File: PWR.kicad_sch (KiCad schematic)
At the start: 37 parts, among them IC1 LMR51460SQDRRRQ1, IC2 TPS628101HQWRWYRQ1, IC3 LP2951-50DRG4, Q1 CSD25483F4, Q2 CSD25483F4

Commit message: improved analogs
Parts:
- added C42, C46: 1uF, Capacitor_SMD:C_0603_1608Metric_Pad1.08x0.95mm_HandSolder, symbol Device:C
- added NT2: NetTie_2, NetTie:NetTie-2_SMD_Pad0.5mm, symbol Device:NetTie_2
- added R13: 100k, Resistor_SMD:R_0603_1608Metric_Pad0.98x0.95mm_HandSolder, symbol Device:R
- C36, C37, C40, C41: footprint Capacitor_SMD:C_0402_1005Metric_Pad0.74x0.62mm_HandSolder -> Capacitor_SMD:C_0603_1608Metric_Pad1.08x0.95mm_HandSolder
- C5: footprint Inductor_SMD:L_1206_3216Metric_Pad1.22x1.90mm_HandSolder -> Capacitor_SMD:C_0603_1608Metric_Pad1.08x0.95mm_HandSolder
- R1, R10, R11, R12, R2, R3, R4, R5, R6, R7, R8, R9: footprint Resistor_SMD:R_0402_1005Metric_Pad0.72x0.64mm_HandSolder -> Resistor_SMD:R_0603_1608Metric_Pad0.98x0.95mm_HandSolder
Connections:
- net +12V is gone; now on net 12V: C33.1, C34.1, C35.1, IC1.10 (VIN_1), IC1.11 (VIN_2), IC1.12 (VIN_3), IC1.9 (EN), R48.1
- net GND: now also C46.2, NT2.1
- net A5V: now reaches IC3.1 (OUTPUT)
- net A5V: now also IC3.2 (SENSE), C42.1
- net AGND: now reaches IC3.3 (SHUTDOWN)
- net AGND: now also IC3.4 (GND), C42.2, NT2.2
- net A5V_PG: now reaches IC3.5 (~{ERROR})
- net A5V_PG: now also R13.1
- net at IC3.6 (VTAP): now also IC3.7 (FEEDBACK)
- net 12V: now reaches IC3.8 (INPUT)
- net 12V: now also C46.1
- net +3V3 renamed 3V3
- net 3V3: now also R13.2
- net +5V renamed 5V
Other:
- moved on the sheet: IC3, R11, R12

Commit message: possible working power mux
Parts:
- removed C33, C34: 4.7uF, Capacitor_SMD:C_1210_3225Metric_Pad1.33x2.70mm_HandSolder, symbol Device:C
- removed C35, C36: 0.1uF, Capacitor_SMD:C_0603_1608Metric_Pad1.08x0.95mm_HandSolder, symbol Device:C
- removed C37: 33pF, Capacitor_SMD:C_0603_1608Metric_Pad1.08x0.95mm_HandSolder, symbol Device:C
- removed C38, C39: 47uF, Capacitor_SMD:C_1210_3225Metric_Pad1.33x2.70mm_HandSolder, symbol Device:C
- removed C40: 4.7nF, Capacitor_SMD:C_0603_1608Metric_Pad1.08x0.95mm_HandSolder, symbol Device:C
- removed C41: 10pF, Capacitor_SMD:C_0603_1608Metric_Pad1.08x0.95mm_HandSolder, symbol Device:C
- removed C42, C46: 1uF, Capacitor_SMD:C_0603_1608Metric_Pad1.08x0.95mm_HandSolder, symbol Device:C
- removed C5, C8: 22uF, Capacitor_SMD:C_0603_1608Metric_Pad1.08x0.95mm_HandSolder, symbol Device:C
- removed C6, C7: 22uF, Inductor_SMD:L_1206_3216Metric_Pad1.22x1.90mm_HandSolder, symbol Device:C
- removed IC1: LMR51460SQDRRRQ1, SON50P300X300X80-13N-D, symbol SamacSys_Parts:LMR51460SQDRRRQ1
- removed IC2: TPS628101HQWRWYRQ1, SamacSys_Parts:TPS6281008QWRWYRQ1, symbol SamacSys_Parts:TPS62810QWRWYRQ1
- removed IC3: LP2951-50DRG4, SOIC127P600X175-8N, symbol 0_SamacSys_Parts:LP2951-50DRG4
- removed L1: 0.47uH, INDPM7066X240N, symbol Device:L
- removed L3: 4.7uH, Inductor_SMD:L_Coilcraft_XAL7030-472, symbol Device:L
- removed NT1: NetTie_2, NetTie:NetTie-2_SMD_Pad0.5mm, symbol Device:NetTie_2
- removed Q1, Q2: CSD25483F4, SamacSys_Parts:CSD25483F4T, symbol SamacSys_Parts:CSD25483F4T
- removed R1, R11, R12, R13, R4, R6: 100k, Resistor_SMD:R_0603_1608Metric_Pad0.98x0.95mm_HandSolder, symbol Device:R
- removed R10: 19.6k, Resistor_SMD:R_0603_1608Metric_Pad0.98x0.95mm_HandSolder, symbol Device:R
- removed R2: 19.1k, Resistor_SMD:R_0603_1608Metric_Pad0.98x0.95mm_HandSolder, symbol Device:R
- removed R3: 1k, Resistor_SMD:R_0603_1608Metric_Pad0.98x0.95mm_HandSolder, symbol Device:R
- removed R5, R7: 10k, Resistor_SMD:R_0603_1608Metric_Pad0.98x0.95mm_HandSolder, symbol Device:R
- removed R8: 8.06k, Resistor_SMD:R_0603_1608Metric_Pad0.98x0.95mm_HandSolder, symbol Device:R
- removed R9: 88.7k, Resistor_SMD:R_0603_1608Metric_Pad0.98x0.95mm_HandSolder, symbol Device:R
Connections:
- no-connect marks 1 -> 0
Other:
- added sheet PWR_3V3 (PWR_3V3.kicad_sch)
- added sheet PWR_A5V (PWR_A5V.kicad_sch)
- added sheet PWR_LV_5V (PWR_LV_5V.kicad_sch)
- added sheet PWR_MUX (PWR_MUX.kicad_sch)
- moved on the sheet: D14, D15, R48, R49

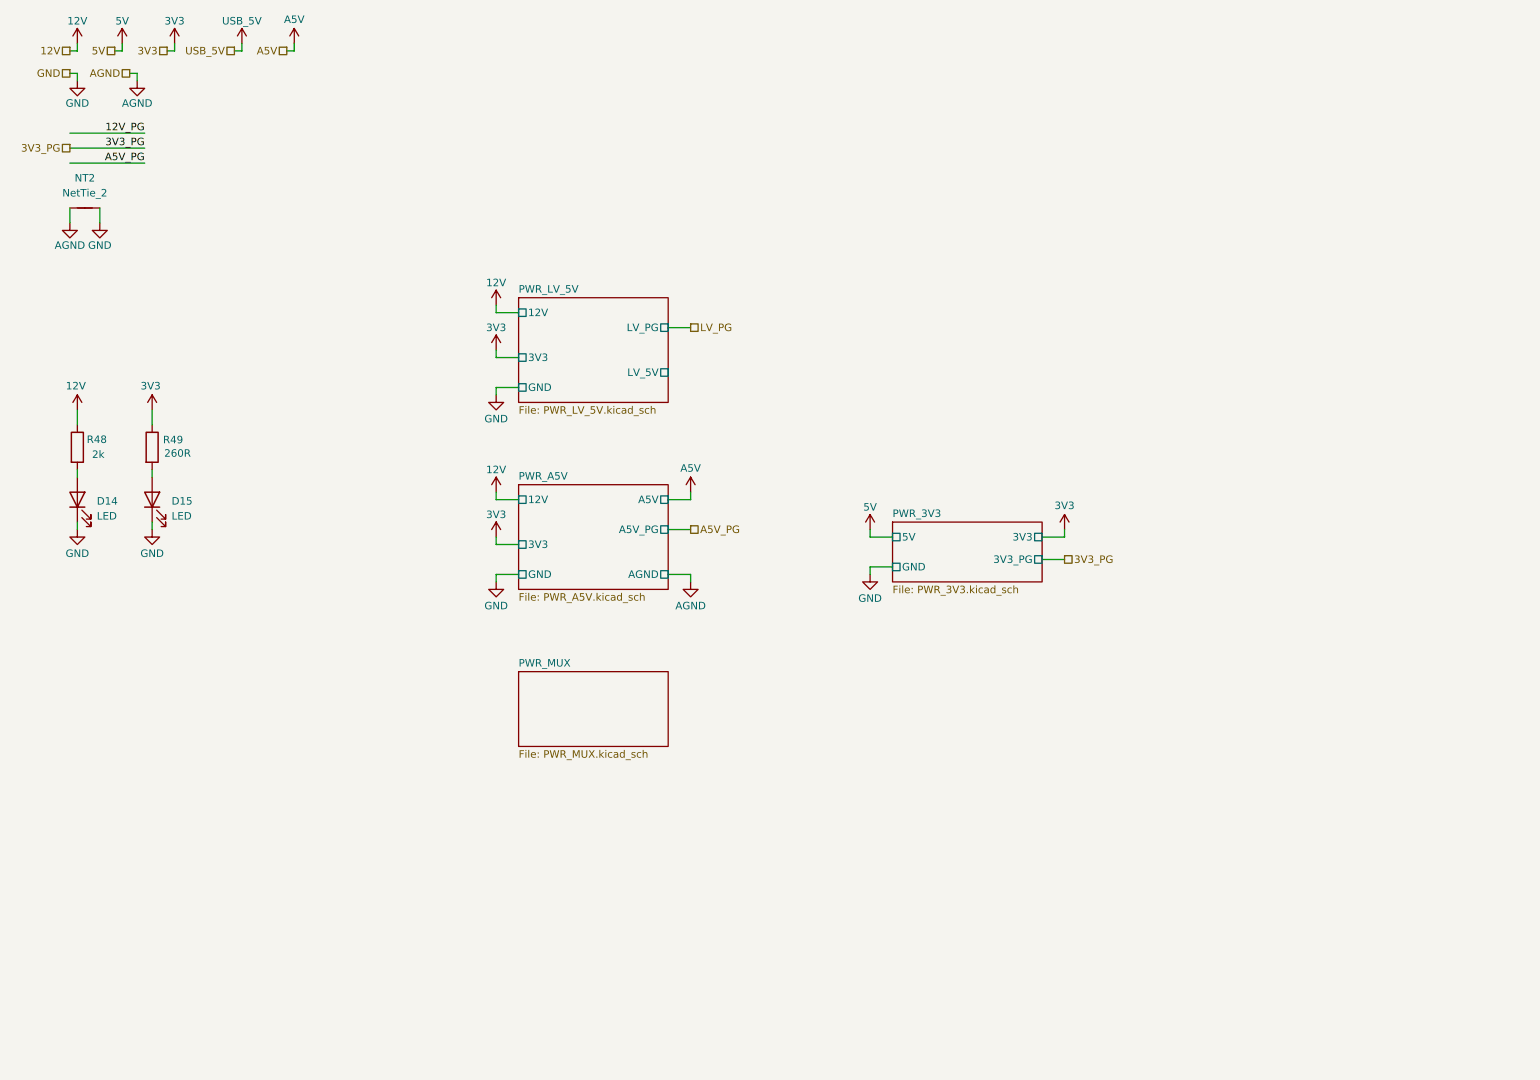
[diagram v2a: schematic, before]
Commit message: updated power layout
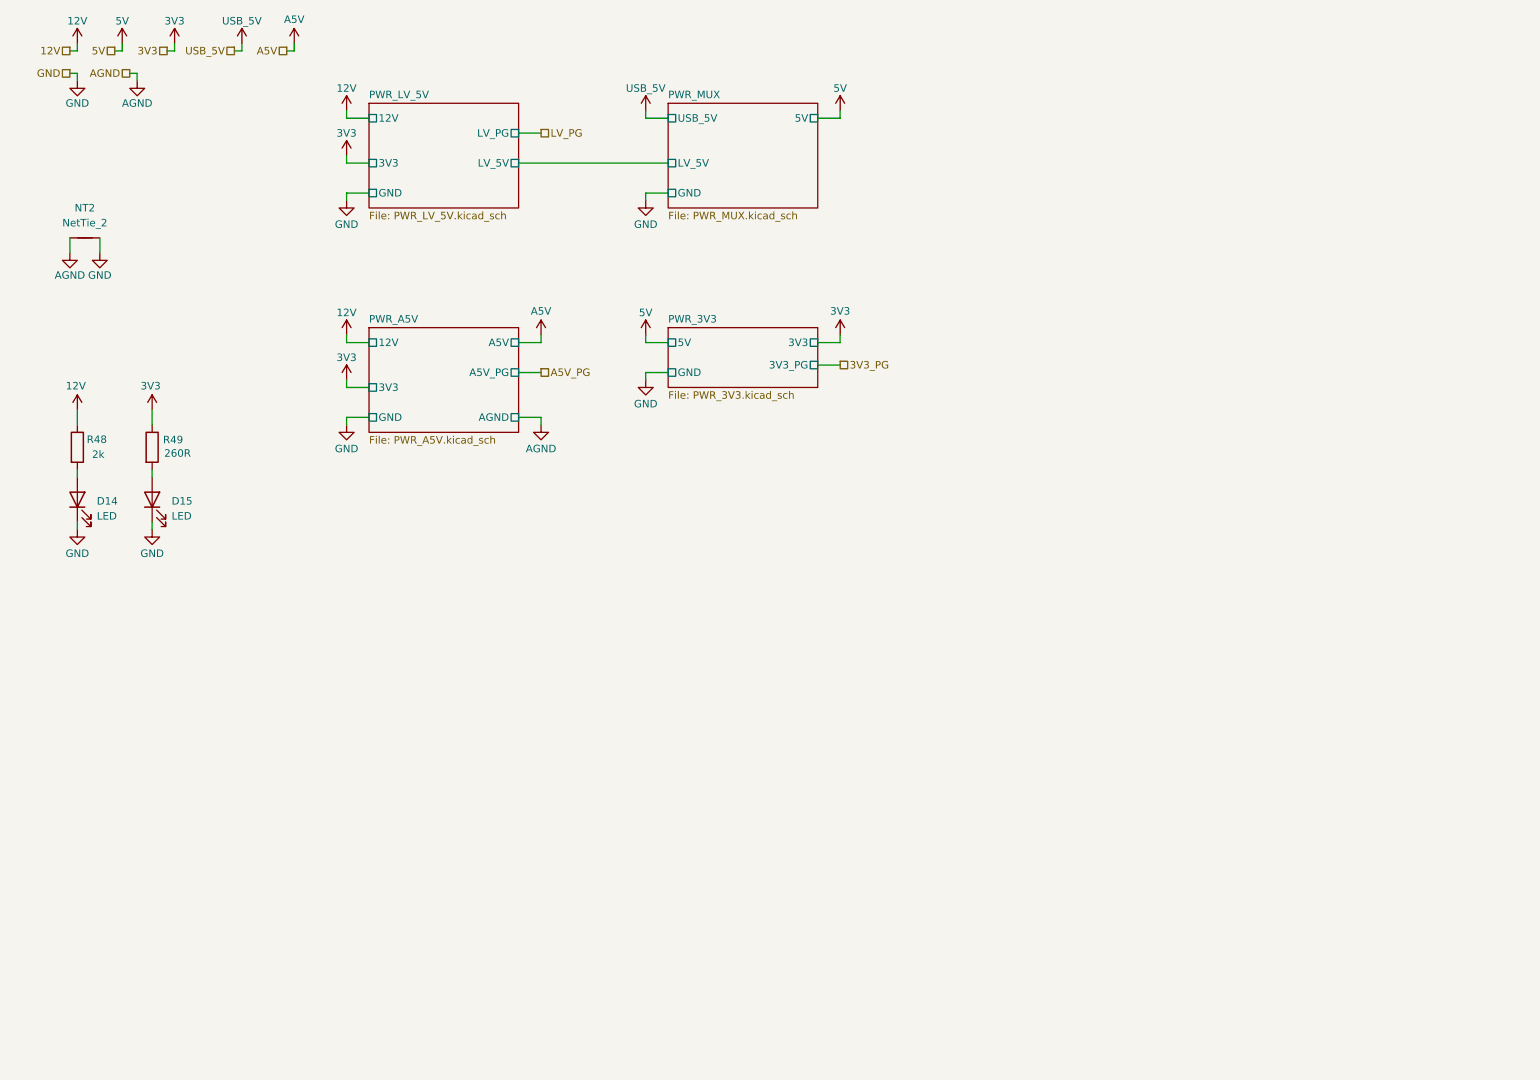
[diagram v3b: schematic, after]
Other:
- sheet PWR_MUX ports: added 5V, GND, LV_5V, USB_5V; removed none
- moved on the sheet: NT2

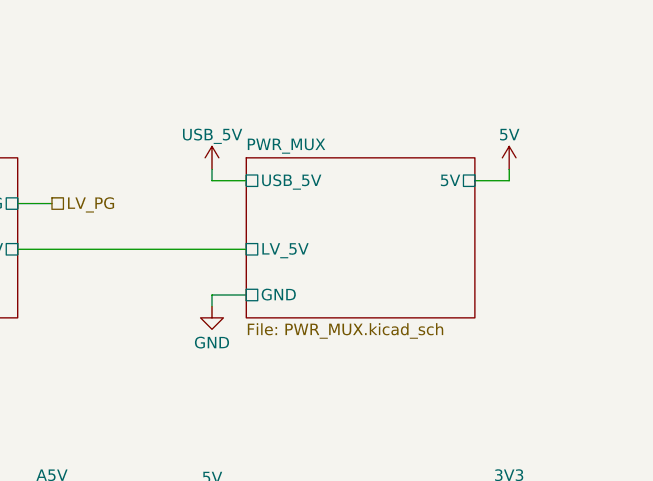
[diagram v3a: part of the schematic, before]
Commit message: added dip switches to wireless disables
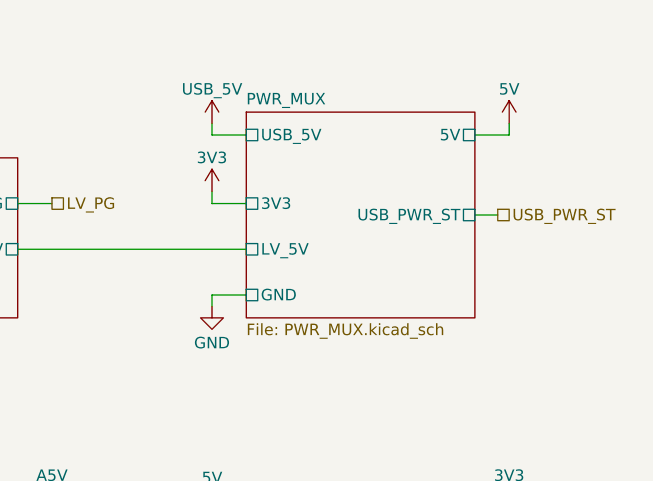
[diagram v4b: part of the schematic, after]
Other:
- sheet PWR_MUX ports: added 3V3, USB_PWR_ST; removed none
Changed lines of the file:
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@@
 	(wire
 		(pts
-			(xy 123.19 31.75) (xy 123.19 33.02)
+			(xy 123.19 26.67) (xy 123.19 27.94)
+		)
+		(stroke
+			(width 0)
+			(type default)
+		)
+	)
+	(wire
+		(pts
+			(xy 123.19 34.29) (xy 123.19 35.56)
 		)
 		(stroke
@@
 	(wire
 		(pts
-			(xy 156.21 31.75) (xy 156.21 33.02)
+			(xy 156.21 26.67) (xy 156.21 27.94)
 		)
 		(stroke
@@
 	(wire
 		(pts
+			(xy 123.19 35.56) (xy 127 35.56)
+		)
+		(stroke
+			(width 0)
+			(type default)
+		)
+	)
+	(wire
+		(pts
 			(xy 72.39 71.12) (xy 76.2 71.12)
 		)
@@
 	(wire
 		(pts
-			(xy 156.21 33.02) (xy 152.4 33.02)
+			(xy 156.21 27.94) (xy 152.4 27.94)
 		)
 		(stroke
@@
 	(wire
 		(pts
-			(xy 123.19 33.02) (xy 127 33.02)
+			(xy 123.19 27.94) (xy 127 27.94)
 		)
 		(stroke
@@
 		(pts
 			(xy 63.5 21.59) (xy 63.5 20.32)
+		)
+		(stroke
+			(width 0)
+			(type default)
+		)
+	)
+	(wire
+		(pts
+			(xy 152.4 36.83) (xy 154.94 36.83)
 		)
 		(stroke
@@
 		)
 	)
+	(hierarchical_label "USB_PWR_ST"
+		(shape passive)
+		(at 154.94 36.83 0)
+		(effects
+			(font
+				(size 1.27 1.27)
+			)
+			(justify left)
+		)
+	)
 	(hierarchical_label "5V"
 		(shape passive)
@@
 	)
 	(symbol
+		(lib_id "power:+12V")
+		(at 123.19 34.29 0)
+		(unit 1)
+		(exclude_from_sim no)
+		(in_bom yes)
+		(on_board yes)
+		(dnp no)
+		(property "Reference" "#PWR0310"
+			(at 123.19 38.1 0)
+			(effects
+				(font
+					(size 1.27 1.27)
+				)
+				(hide yes)
+			)
+		)
+		(property "Value" "3V3"
+			(at 123.19 30.48 0)
+			(effects
+				(font
+					(size 1.27 1.27)
+				)
+			)
+		)
+		(property "Footprint" ""
+			(at 123.19 34.29 0)
+			(effects
+				(font
+					(size 1.27 1.27)
+				)
+				(hide yes)
+			)
+		)
+		(property "Datasheet" ""
+			(at 123.19 34.29 0)
+			(effects
+				(font
+					(size 1.27 1.27)
+				)
+				(hide yes)
+			)
+		)
+		(property "Description" "Power symbol creates a global label with name \"+12V\""
+			(at 123.19 34.29 0)
+			(effects
+				(font
+					(size 1.27 1.27)
+				)
+				(hide yes)
+			)
+		)
+		(pin "1"
+		)
+		(instances
+			(project "NCU"
+				(path "/3aee14c3-5480-4f7c-989e-3fef81779034/05e3be97-98f6-4518-a1a7-240d4da327e6"
+					(reference "#PWR0310")
+					(unit 1)
+				)
+			)
+		)
+	)
+	(symbol
 		(lib_id "power:GND")
 		(at 30.48 55.88 0)
@@
 	(symbol
 		(lib_id "power:+12V")
-		(at 156.21 31.75 0)
+		(at 156.21 26.67 0)
 		(mirror y)
 		(unit 1)
@@
 		(dnp no)
 		(property "Reference" "#PWR0295"
-			(at 156.21 35.56 0)
+			(at 156.21 30.48 0)
 			(effects
 				(font
@@
 		)
 		(property "Value" "5V"
-			(at 156.21 27.94 0)
+			(at 156.21 22.86 0)
 			(effects
 				(font
@@
 		)
 		(property "Footprint" ""
-			(at 156.21 31.75 0)
+			(at 156.21 26.67 0)
 			(effects
 				(font
@@
 		)
 		(property "Datasheet" ""
-			(at 156.21 31.75 0)
+			(at 156.21 26.67 0)
 			(effects
 				(font
@@
 		)
 		(property "Description" "Power symbol creates a global label with name \"+12V\""
-			(at 156.21 31.75 0)
+			(at 156.21 26.67 0)
 			(effects
 				(font
@@
 	(symbol
 		(lib_id "power:+12V")
-		(at 123.19 31.75 0)
+		(at 123.19 26.67 0)
 		(unit 1)
 		(exclude_from_sim no)
@@
 		(dnp no)
 		(property "Reference" "#PWR0297"
-			(at 123.19 35.56 0)
+			(at 123.19 30.48 0)
 			(effects
 				(font
@@
 		)
 		(property "Value" "USB_5V"
-			(at 123.19 27.94 0)
+			(at 123.19 22.86 0)
 			(effects
 				(font
@@
 		)
 		(property "Footprint" ""
-			(at 123.19 31.75 0)
+			(at 123.19 26.67 0)
 			(effects
 				(font
@@
 		)
 		(property "Datasheet" ""
-			(at 123.19 31.75 0)
+			(at 123.19 26.67 0)
 			(effects
 				(font
@@
 		)
 		(property "Description" "Power symbol creates a global label with name \"+12V\""
-			(at 123.19 31.75 0)
+			(at 123.19 26.67 0)
 			(effects
 				(font
@@
 	)
 	(sheet
-		(at 127 30.48)
-		(size 25.4 17.78)
+		(at 127 25.4)
+		(size 25.4 22.86)
 		(exclude_from_sim no)
 		(in_bom yes)
@@
 		)
 		(property "Sheetname" "PWR_MUX"
-			(at 127 29.7684 0)
+			(at 127 24.6884 0)
 			(effects
 				(font
@@
 		)
 		(pin "5V" passive
-			(at 152.4 33.02 0)
+			(at 152.4 27.94 0)
 			(effects
 				(font
@@
 		)
 		(pin "USB_5V" passive
-			(at 127 33.02 180)
+			(at 127 27.94 180)
 			(effects
 				(font
@@
 			)
 		)
+		(pin "3V3" passive
+			(at 127 35.56 180)
+			(effects
+				(font
+					(size 1.27 1.27)
+				)
+				(justify left)
+			)
+		)
+		(pin "USB_PWR_ST" passive
+			(at 152.4 36.83 0)
+			(effects
+				(font
+					(size 1.27 1.27)
+				)
+				(justify right)
+			)
+		)

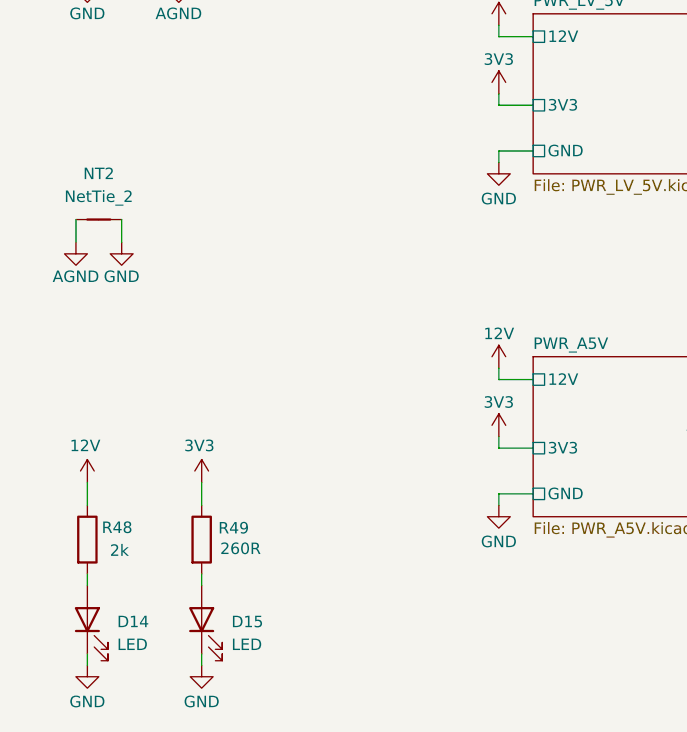
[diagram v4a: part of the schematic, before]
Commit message: redid annotations, added test point
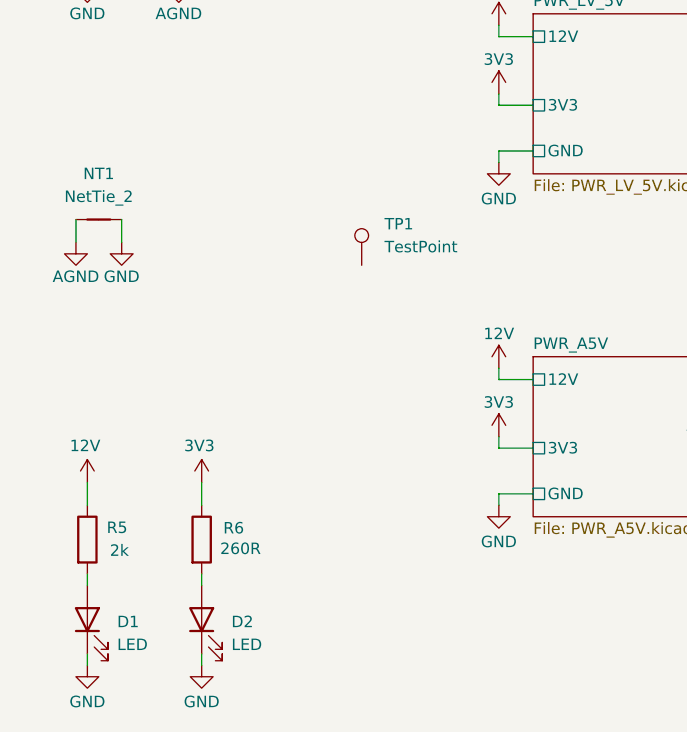
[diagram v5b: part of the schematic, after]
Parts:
- added TP1: TestPoint, TestPoint:TestPoint_THTPad_D2.0mm_Drill1.0mm, symbol Connector:TestPoint
- renumbered D14 to D1, D15 to D2, NT2 to NT1, R48 to R5, R49 to R6
